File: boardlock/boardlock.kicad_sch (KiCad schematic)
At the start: 0 parts

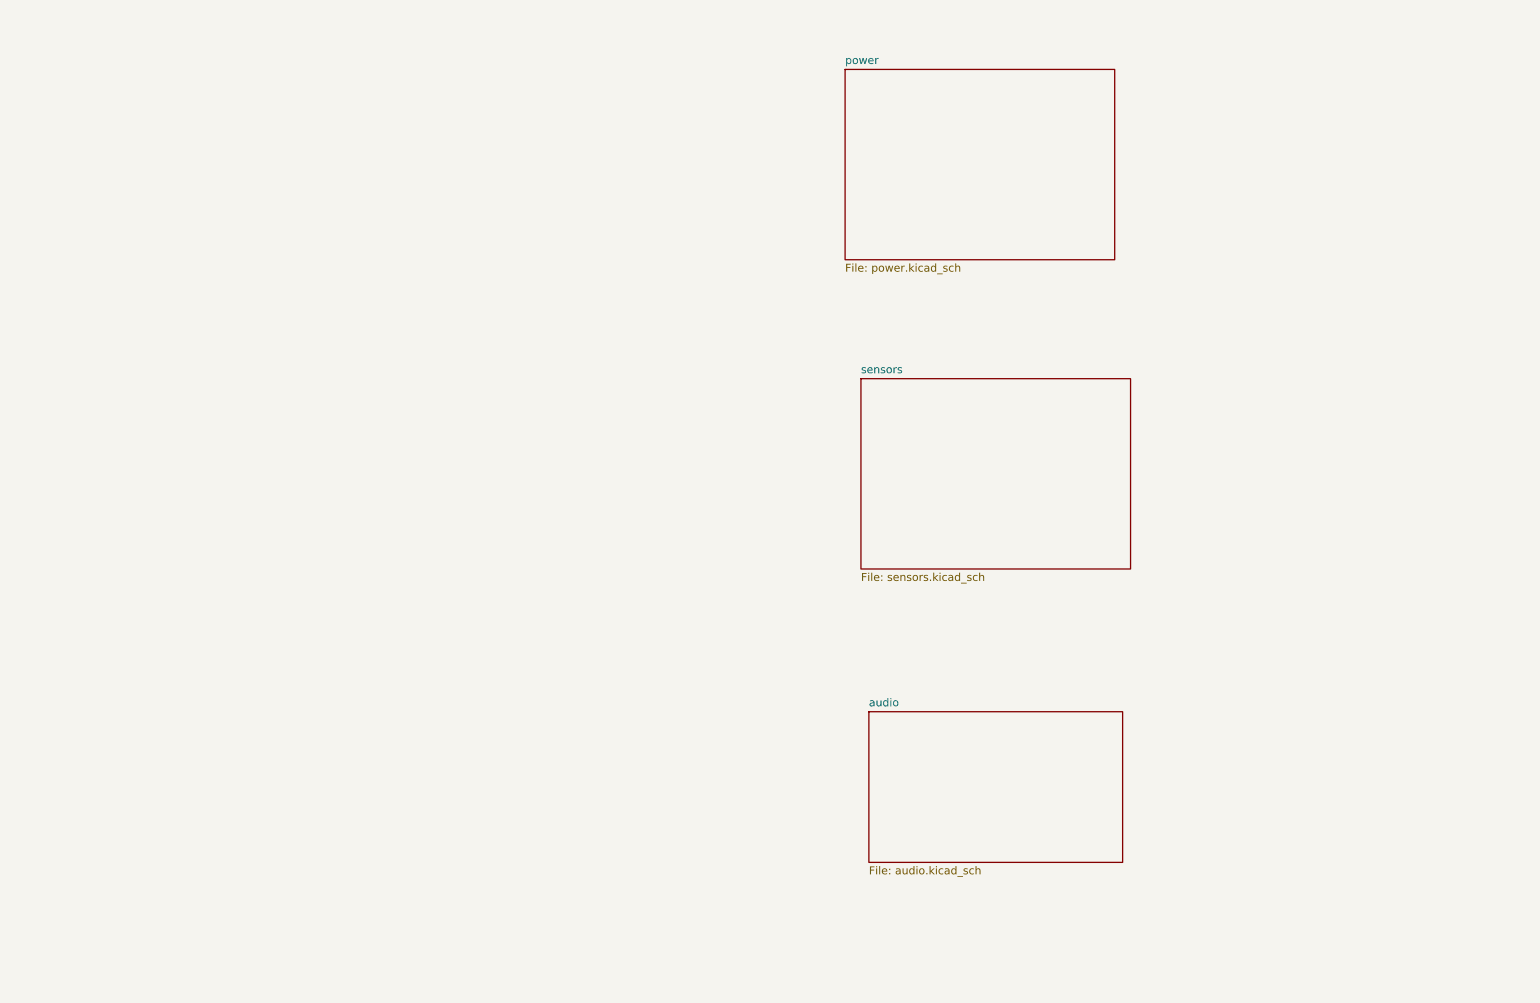
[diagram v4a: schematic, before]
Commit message: Added ESP32 library and SCH edits
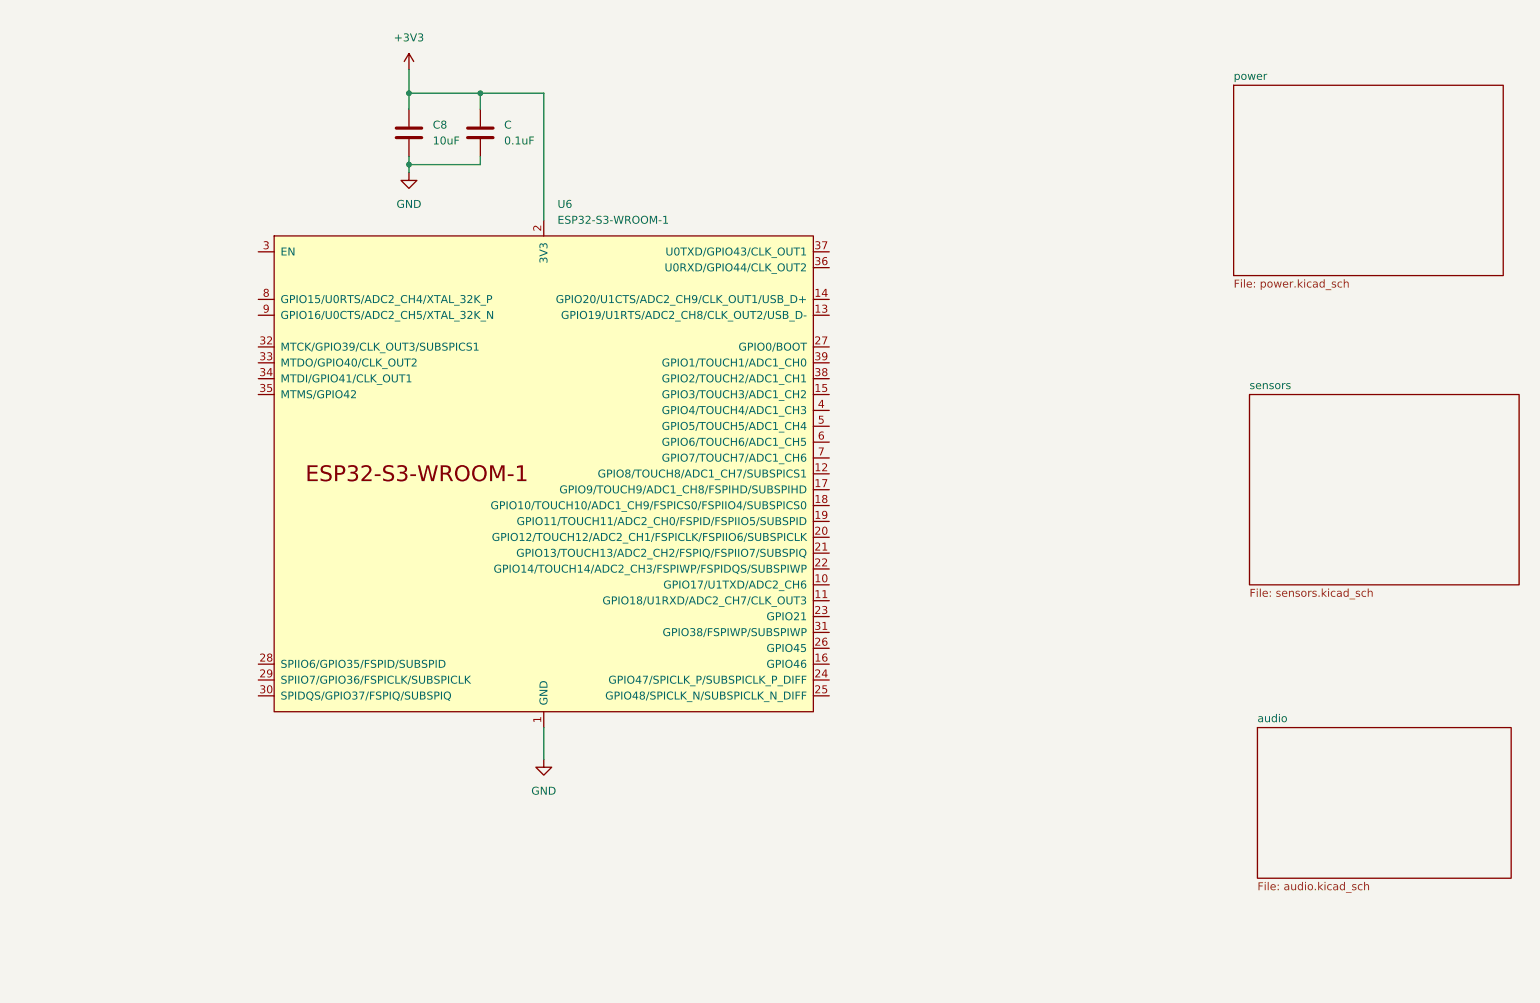
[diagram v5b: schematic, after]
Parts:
- added C: 0.1uF, symbol Device:C
- added C8: 10uF, symbol Device:C
- added U6: ESP32-S3-WROOM-1, PCM_Espressif:ESP32-S3-WROOM-1, symbol PCM_Espressif:ESP32-S3-WROOM-1
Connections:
- new net +3V3: C.1, C8.1, U6.2 (3V3)
- new net GND: C.2, C8.2, U6.1 (GND), U6.40 (GND), U6.41 (GND)
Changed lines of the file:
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@@
 (kicad_sch (version 20230121) (generator eeschema)
   (paper "A4")
-  (sheet (at 153.67 128.27) (size 40.64 24.13) (fields_autoplaced)
+  (junction (at 80.01 40.64) (diameter 0) (color 0 0 0 0)
+  )
+  (junction (at 91.44 29.21) (diameter 0) (color 0 0 0 0)
+  )
+  (junction (at 80.01 29.21) (diameter 0) (color 0 0 0 0)
+  )
+  (wire (pts (xy 80.01 39.37) (xy 80.01 40.64))
+    (stroke (width 0) (type default))
+  )
+  (wire (pts (xy 80.01 29.21) (xy 80.01 31.75))
+    (stroke (width 0) (type default))
+  )
+  (wire (pts (xy 91.44 40.64) (xy 91.44 39.37))
+    (stroke (width 0) (type default))
+  )
+  (wire (pts (xy 80.01 40.64) (xy 80.01 41.91))
+    (stroke (width 0) (type default))
+  )
+  (wire (pts (xy 91.44 29.21) (xy 101.6 29.21))
+    (stroke (width 0) (type default))
+  )
+  (wire (pts (xy 101.6 130.81) (xy 101.6 135.89))
+    (stroke (width 0) (type default))
+  )
+  (wire (pts (xy 80.01 25.4) (xy 80.01 29.21))
+    (stroke (width 0) (type default))
+  )
+  (wire (pts (xy 80.01 29.21) (xy 91.44 29.21))
+    (stroke (width 0) (type default))
+  )
+  (wire (pts (xy 80.01 40.64) (xy 91.44 40.64))
+    (stroke (width 0) (type default))
+  )
+  (wire (pts (xy 101.6 29.21) (xy 101.6 49.53))
+    (stroke (width 0) (type default))
+  )
+  (wire (pts (xy 91.44 29.21) (xy 91.44 31.75))
+    (stroke (width 0) (type default))
+  )
+  (symbol (lib_id "power:GND") (at 80.01 41.91 0) (unit 1)
+    (in_bom yes) (on_board yes) (dnp no) (fields_autoplaced)
+    (property "Reference" "#PWR021" (at 80.01 48.26 0)
+      (effects (font (size 1.27 1.27)) hide)
+    )
+    (property "Value" "GND" (at 80.01 46.99 0)
+      (effects (font (size 1.27 1.27)))
+    )
+    (property "Footprint" "" (at 80.01 41.91 0)
+      (effects (font (size 1.27 1.27)) hide)
+    )
+    (property "Datasheet" "" (at 80.01 41.91 0)
+      (effects (font (size 1.27 1.27)) hide)
+    )
+    (pin "1")
+    (instances
+      (project "boardlock"
+        (path "/e1fc29ce-837e-4062-84d8-c7e423f9eab9"
+          (reference "#PWR021") (unit 1)
+        )
+      )
+    )
+  )
+  (symbol (lib_id "PCM_Espressif:ESP32-S3-WROOM-1") (at 101.6 90.17 0) (unit 1)
+    (in_bom yes) (on_board yes) (dnp no) (fields_autoplaced)
+    (property "Reference" "U6" (at 103.7941 46.99 0)
+      (effects (font (size 1.27 1.27)) (justify left))
+    )
+    (property "Value" "ESP32-S3-WROOM-1" (at 103.7941 49.53 0)
+      (effects (font (size 1.27 1.27)) (justify left))
+    )
+    (property "Footprint" "PCM_Espressif:ESP32-S3-WROOM-1" (at 104.14 138.43 0)
+      (effects (font (size 1.27 1.27)) hide)
+    )
+    (property "Datasheet" "https://www.espressif.com/sites/default/files/documentation/esp32-s3-wroom-1_wroom-1u_datasheet_en.pdf" (at 104.14 140.97 0)
+      (effects (font (size 1.27 1.27)) hide)
+    )
+    (pin "1")
+    (pin "10")
+    (pin "11")
+    (pin "12")
+    (pin "13")
+    (pin "14")
+    (pin "15")
+    (pin "16")
+    (pin "17")
+    (pin "18")
+    (pin "19")
+    (pin "2")
+    (pin "20")
+    (pin "21")
+    (pin "22")
+    (pin "23")
+    (pin "24")
+    (pin "25")
+    (pin "26")
+    (pin "27")
+    (pin "28")
+    (pin "29")
+    (pin "3")
+    (pin "30")
+    (pin "31")
+    (pin "32")
+    (pin "33")
+    (pin "34")
+    (pin "35")
+    (pin "36")
+    (pin "37")
+    (pin "38")
+    (pin "39")
+    (pin "4")
+    (pin "40")
+    (pin "41")
+    (pin "5")
+    (pin "6")
+    (pin "7")
+    (pin "8")
+    (pin "9")
+    (instances
+      (project "boardlock"
+        (path "/e1fc29ce-837e-4062-84d8-c7e423f9eab9"
+          (reference "U6") (unit 1)
+        )
+      )
+    )
+  )
+  (symbol (lib_id "power:+3V3") (at 80.01 25.4 0) (unit 1)
+    (in_bom yes) (on_board yes) (dnp no) (fields_autoplaced)
+    (property "Reference" "#PWR019" (at 80.01 29.21 0)
+      (effects (font (size 1.27 1.27)) hide)
+    )
+    (property "Value" "+3V3" (at 80.01 20.32 0)
+      (effects (font (size 1.27 1.27)))
+    )
+    (property "Footprint" "" (at 80.01 25.4 0)
+      (effects (font (size 1.27 1.27)) hide)
+    )
+    (property "Datasheet" "" (at 80.01 25.4 0)
+      (effects (font (size 1.27 1.27)) hide)
+    )
+    (pin "1")
+    (instances
+      (project "boardlock"
+        (path "/e1fc29ce-837e-4062-84d8-c7e423f9eab9"
+          (reference "#PWR019") (unit 1)
+        )
+      )
+    )
+  )
+  (symbol (lib_id "power:GND") (at 101.6 135.89 0) (unit 1)
+    (in_bom yes) (on_board yes) (dnp no) (fields_autoplaced)
+    (property "Reference" "#PWR020" (at 101.6 142.24 0)
+      (effects (font (size 1.27 1.27)) hide)
+    )
+    (property "Value" "GND" (at 101.6 140.97 0)
+      (effects (font (size 1.27 1.27)))
+    )
+    (property "Footprint" "" (at 101.6 135.89 0)
+      (effects (font (size 1.27 1.27)) hide)
+    )
+    (property "Datasheet" "" (at 101.6 135.89 0)
+      (effects (font (size 1.27 1.27)) hide)
+    )
+    (pin "1")
+    (instances
+      (project "boardlock"
+        (path "/e1fc29ce-837e-4062-84d8-c7e423f9eab9"
+          (reference "#PWR020") (unit 1)
+        )
+      )
+    )
+  )
+  (symbol (lib_id "Device:C") (at 80.01 35.56 0) (unit 1)
+    (in_bom yes) (on_board yes) (dnp no) (fields_autoplaced)
+    (property "Reference" "C8" (at 83.82 34.29 0)
+      (effects (font (size 1.27 1.27)) (justify left))
+    )
+    (property "Value" "10uF" (at 83.82 36.83 0)
+      (effects (font (size 1.27 1.27)) (justify left))
+    )
+    (property "Footprint" "" (at 80.9752 39.37 0)
+      (effects (font (size 1.27 1.27)) hide)
+    )
+    (property "Datasheet" "~" (at 80.01 35.56 0)
+      (effects (font (size 1.27 1.27)) hide)
+    )
+    (pin "1")
+    (pin "2")
+    (instances
+      (project "boardlock"
+        (path "/e1fc29ce-837e-4062-84d8-c7e423f9eab9"
+          (reference "C8") (unit 1)
+        )
+      )
+    )
+  )
+  (symbol (lib_id "Device:C") (at 91.44 35.56 0) (unit 1)
+    (in_bom yes) (on_board yes) (dnp no) (fields_autoplaced)
+    (property "Reference" "C" (at 95.25 34.29 0)
+      (effects (font (size 1.27 1.27)) (justify left))
+    )
+    (property "Value" "0.1uF" (at 95.25 36.83 0)
+      (effects (font (size 1.27 1.27)) (justify left))
+    )
+    (property "Footprint" "" (at 92.4052 39.37 0)
+      (effects (font (size 1.27 1.27)) hide)
+    )
+    (property "Datasheet" "~" (at 91.44 35.56 0)
+      (effects (font (size 1.27 1.27)) hide)
+    )
+    (pin "1")
+    (pin "2")
+    (instances
+      (project "boardlock"
+        (path "/e1fc29ce-837e-4062-84d8-c7e423f9eab9"
+          (reference "C") (unit 1)
+        )
+      )
+    )
+  )
+  (sheet (at 215.9 130.81) (size 40.64 24.13) (fields_autoplaced)
     (stroke (width 0.1524) (type solid))
     (fill (color 0 0 0 0.0000))
-    (property "Sheetname" "audio" (at 153.67 127.5584 0)
+    (property "Sheetname" "audio" (at 215.9 130.0984 0)
       (effects (font (size 1.27 1.27)) (justify left bottom))
     )
-    (property "Sheetfile" "audio.kicad_sch" (at 153.67 152.9846 0)
+    (property "Sheetfile" "audio.kicad_sch" (at 215.9 155.5246 0)
       (effects (font (size 1.27 1.27)) (justify left top))
     )
@@
     )
   )
-  (sheet (at 149.86 25.4) (size 43.18 30.48) (fields_autoplaced)
+  (sheet (at 212.09 27.94) (size 43.18 30.48) (fields_autoplaced)
     (stroke (width 0.1524) (type solid))
     (fill (color 0 0 0 0.0000))
-    (property "Sheetname" "power" (at 149.86 24.6884 0)
+    (property "Sheetname" "power" (at 212.09 27.2284 0)
       (effects (font (size 1.27 1.27)) (justify left bottom))
     )
-    (property "Sheetfile" "power.kicad_sch" (at 149.86 56.4646 0)
+    (property "Sheetfile" "power.kicad_sch" (at 212.09 59.0046 0)
       (effects (font (size 1.27 1.27)) (justify left top))
     )
@@
     )
   )
-  (sheet (at 152.4 74.93) (size 43.18 30.48) (fields_autoplaced)
+  (sheet (at 214.63 77.47) (size 43.18 30.48) (fields_autoplaced)
     (stroke (width 0.1524) (type solid))
     (fill (color 0 0 0 0.0000))
-    (property "Sheetname" "sensors" (at 152.4 74.2184 0)
+    (property "Sheetname" "sensors" (at 214.63 76.7584 0)
       (effects (font (size 1.27 1.27)) (justify left bottom))
     )
-    (property "Sheetfile" "sensors.kicad_sch" (at 152.4 105.9946 0)
+    (property "Sheetfile" "sensors.kicad_sch" (at 214.63 108.5346 0)
       (effects (font (size 1.27 1.27)) (justify left top))
     )

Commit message: ESP32 connection edits
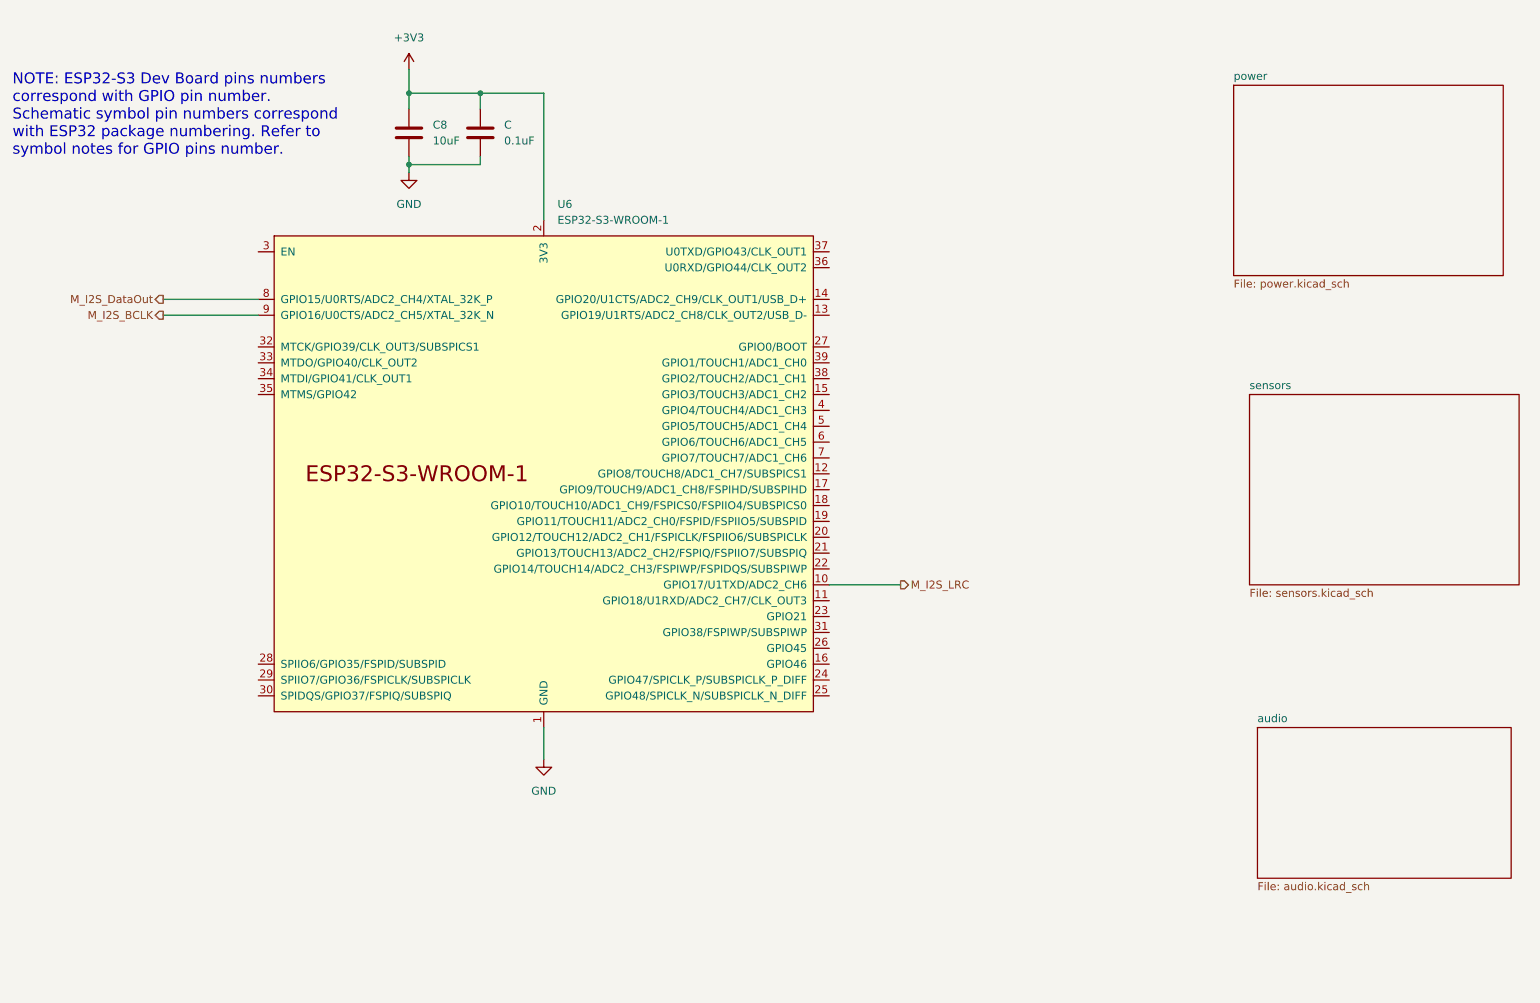
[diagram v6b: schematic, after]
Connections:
- net M_I2S_LRC: now reaches U6.10 (GPIO17/U1TXD/ADC2_CH6)
- net M_I2S_DataOut: now reaches U6.8 (GPIO15/U0RTS/ADC2_CH4/XTAL_32K_P)
- net M_I2S_BCLK: now reaches U6.9 (GPIO16/U0CTS/ADC2_CH5/XTAL_32K_N)
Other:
- note added: "NOTE: ESP32-S3 Dev Board pins numbers correspond with GPIO pin number. Schematic symbol pin numbers correspond with ESP32 package numbering. Refer to symbol notes for GPIO pins number."
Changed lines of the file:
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@@
+    (stroke (width 0) (type default))
+  )
+  (wire (pts (xy 40.64 64.77) (xy 55.88 64.77))
     (stroke (width 0) (type default))
   )
@@
   )
   (wire (pts (xy 91.44 40.64) (xy 91.44 39.37))
+    (stroke (width 0) (type default))
+  )
+  (wire (pts (xy 40.64 62.23) (xy 55.88 62.23))
     (stroke (width 0) (type default))
   )
@@
     (stroke (width 0) (type default))
   )
+  (wire (pts (xy 147.32 107.95) (xy 158.75 107.95))
+    (stroke (width 0) (type default))
+  )
+  (text "NOTE: ESP32-S3 Dev Board pins numbers\ncorrespond with GPIO pin number.\nSchematic symbol pin numbers correspond\nwith ESP32 package numbering. Refer to\nsymbol notes for GPIO pins number."
+    (at 16.51 39.37 0)
+    (effects (font (size 1.75 1.75)) (justify left bottom))
+  )
+  (hierarchical_label "M_I2S_DataOut" (shape output) (at 40.64 62.23 180) (fields_autoplaced)
+    (effects (font (size 1.27 1.27)) (justify right))
+  )
+  (hierarchical_label "M_I2S_LRC" (shape output) (at 158.75 107.95 0) (fields_autoplaced)
+    (effects (font (size 1.27 1.27)) (justify left))
+  )
+  (hierarchical_label "M_I2S_BCLK" (shape output) (at 40.64 64.77 180) (fields_autoplaced)
+    (effects (font (size 1.27 1.27)) (justify right))
+  )
   (symbol (lib_id "power:GND") (at 80.01 41.91 0) (unit 1)
